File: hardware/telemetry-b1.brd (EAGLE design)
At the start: 63.5 x 76.2 mm, 119 parts, among them IC1 COPERNICUSSMD, IC10 TPS70933, IC2 TPS70933, IC4 STM32L073CZT6, IC5 TPS62160, IC6 HX1, IC7 LMP7702, IC9 HIH9131, J1 I2C1, J10 TEMP_BAT, J11 DNP, J12 INSOL, J13 SMA_EDGE, J2 I2C2, J3 SMA_EDGE, J4 USD-SOCKET, J5 BAT, J6 SMA_EDGE, J7 SMA_EDGE, J8 TEMP_GPS, J9 TEMP_HOT, K1 ARE104H, K2 ARE104H, Q1 AO3400A, Q2 AO3400A, U1 LTC3105, U2 INA219, Y1 32768, Y2 8M

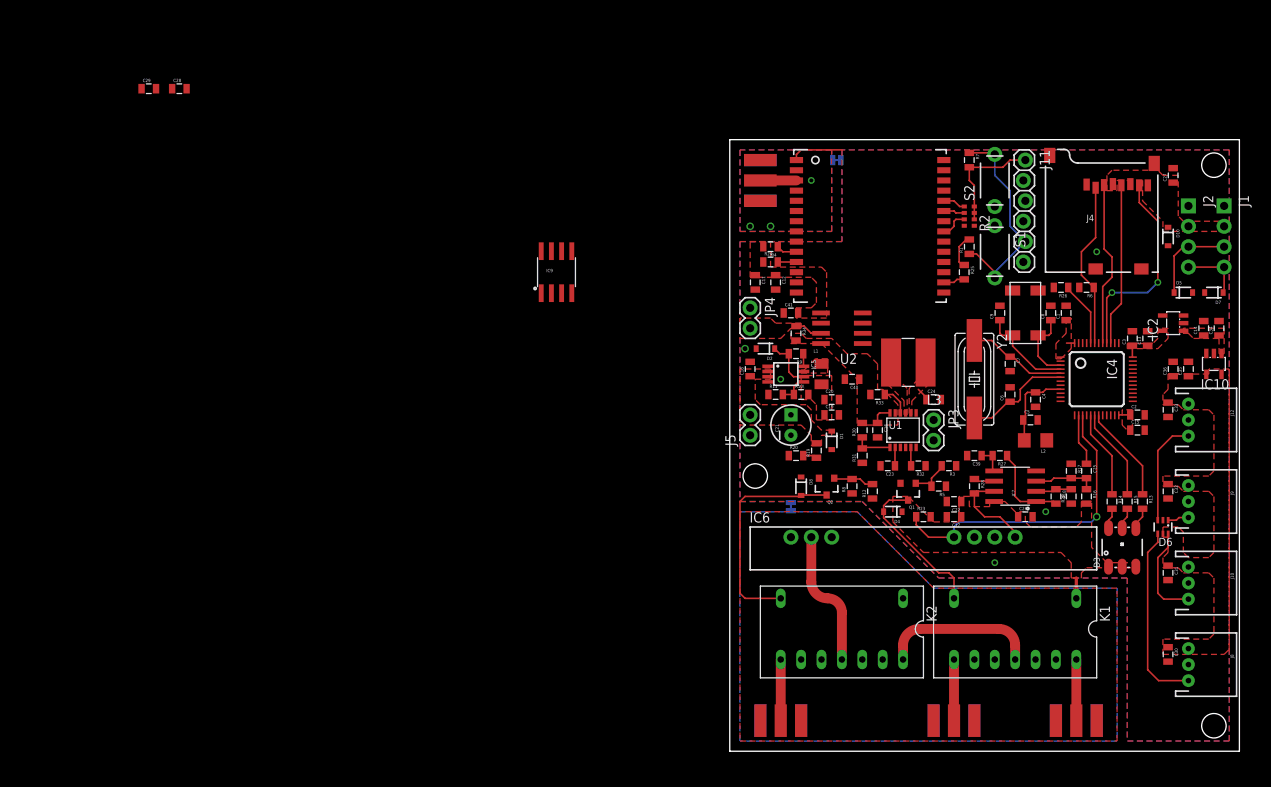
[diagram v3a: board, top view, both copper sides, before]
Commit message: Work on layout on beta PCB. Need to swap i2c and swd headers
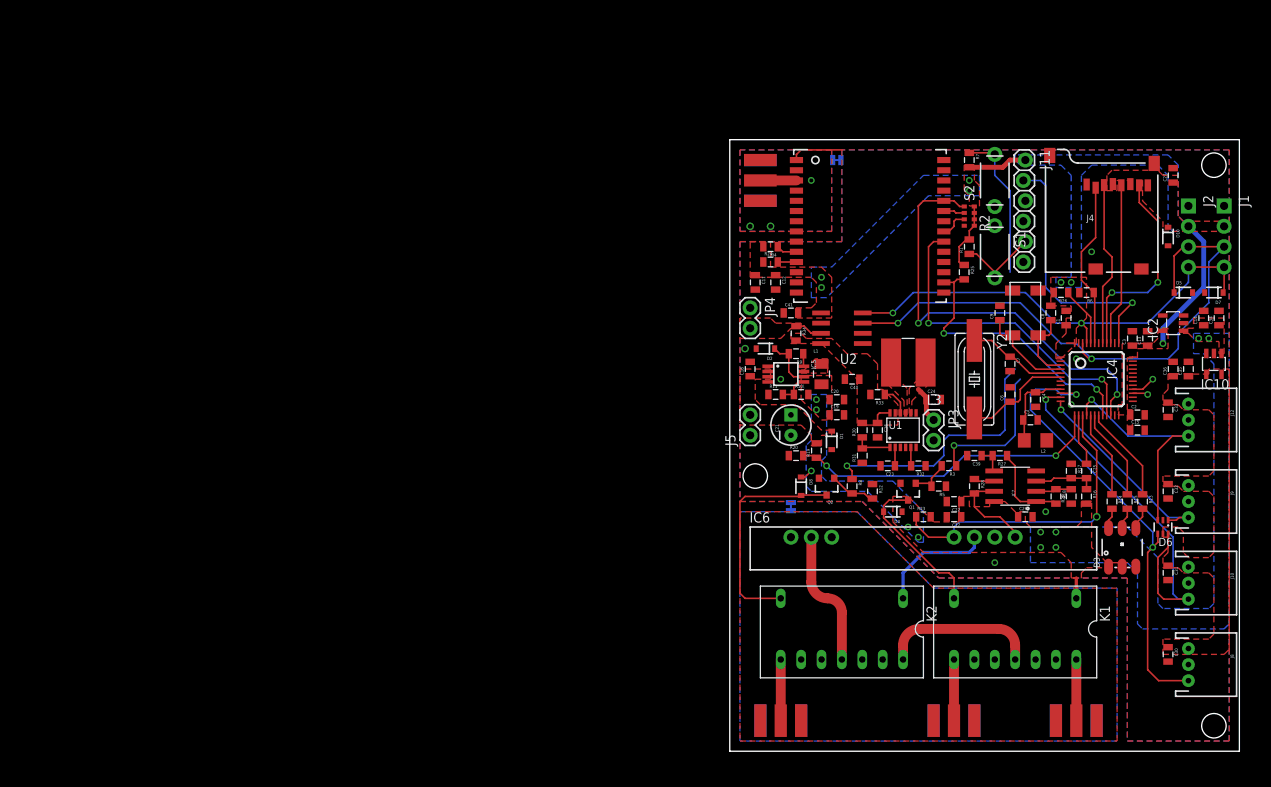
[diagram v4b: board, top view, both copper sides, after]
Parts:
- removed C28, C29: 0.1u, SparkFun-Passives:0805
- removed IC9: HIH9131, SparkFun-AnalogIC:SOIC8
- added U$2: (no value), HAB:GARAGE
- added U$5: (no value), HAB:MSFT_LOGO
- moved FRAME2 85.9 mm to (0.00, 77.5)
- moved FRAME1 84.6 mm to (1.27, 77.5)
- moved C14 1.27 mm to (59.1, 54.0)
- moved C34 1.27 mm to (61.0, 54.0)
- moved C19 0.64 mm to (13.3, 41.9)
- moved C20 0.64 mm to (13.3, 43.8)
- moved C1 0.63 mm to (41.9, 54.0)
- moved R26 0.63 mm to (41.3, 57.1)
- moved R6 0.63 mm to (44.5, 57.1)
- turned R12 to 270 degrees
- turned R8 to 270 degrees
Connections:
- removed net AL_L: IC9.6
- removed net VCORE: C28.1, IC9.1
- net 3.3V: now also R2.1
- net CSHUM: no longer IC9.3
- net GND: no longer C28.2, C29.2, IC9.2
- net MISO: no longer IC9.5
- net SCK: no longer IC9.4
- net VS: no longer C29.1, IC9.8
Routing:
- net SDA: track 11.3 -> 72.7 mm, vias 0 -> 2
- net GPSRX: track 2.84 -> 54.4 mm, vias 0 -> 2
- net SCL: track 7.67 -> 57.6 mm, vias 0 -> 2
- net GPSTX: track 0.00 -> 40.9 mm, vias 0 -> 2
- net VDIV: track 1.75 -> 39.6 mm, vias 0 -> 2
- net RS1: track 0.00 -> 35.7 mm, vias 0 -> 2
- net TEMPB: track 12.0 -> 47.0 mm, vias 0 -> 1
- net TEMPG: track 23.1 -> 56.7 mm, vias 0 -> 2
- net SWCLK: track 0.00 -> 33.1 mm, vias 0 -> 1
- net XSTBY: track 2.69 -> 35.1 mm, vias 0 -> 2
- net PHOTO: track 2.66 -> 25.2 mm, vias 0 -> 1
- net RS0: track 0.00 -> 20.0 mm, vias 0 -> 2
- net 5V: track 8.91 -> 25.1 mm, vias 0 -> 11
- net INSOL: track 13.2 -> 29.4 mm, vias 0 -> 1
- net 3.3V: track 22.0 -> 34.6 mm, vias 0 -> 7
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- added copper zone on layer 16, net 3.3V
- added copper zone on layer 16, net 5V

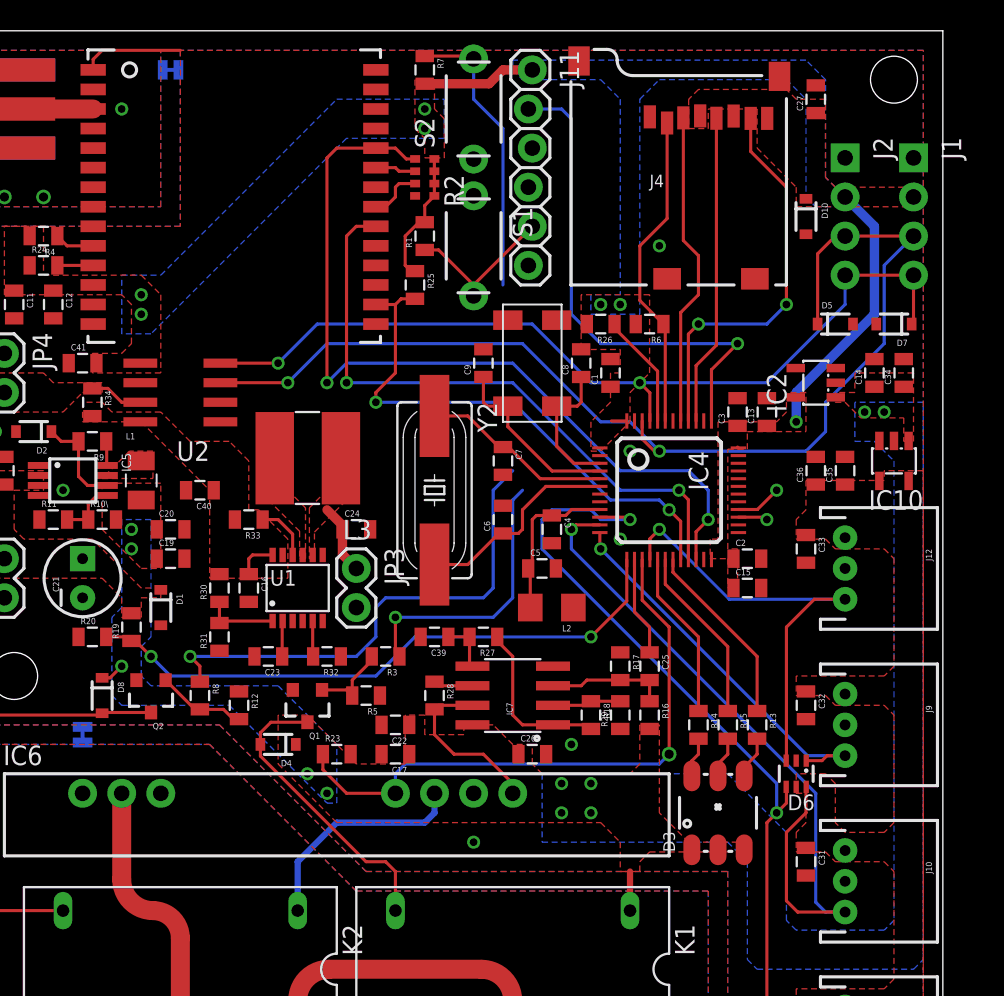
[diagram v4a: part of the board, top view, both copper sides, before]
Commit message: Finish routing all traces on beta board. Needs a silkscreen pass.
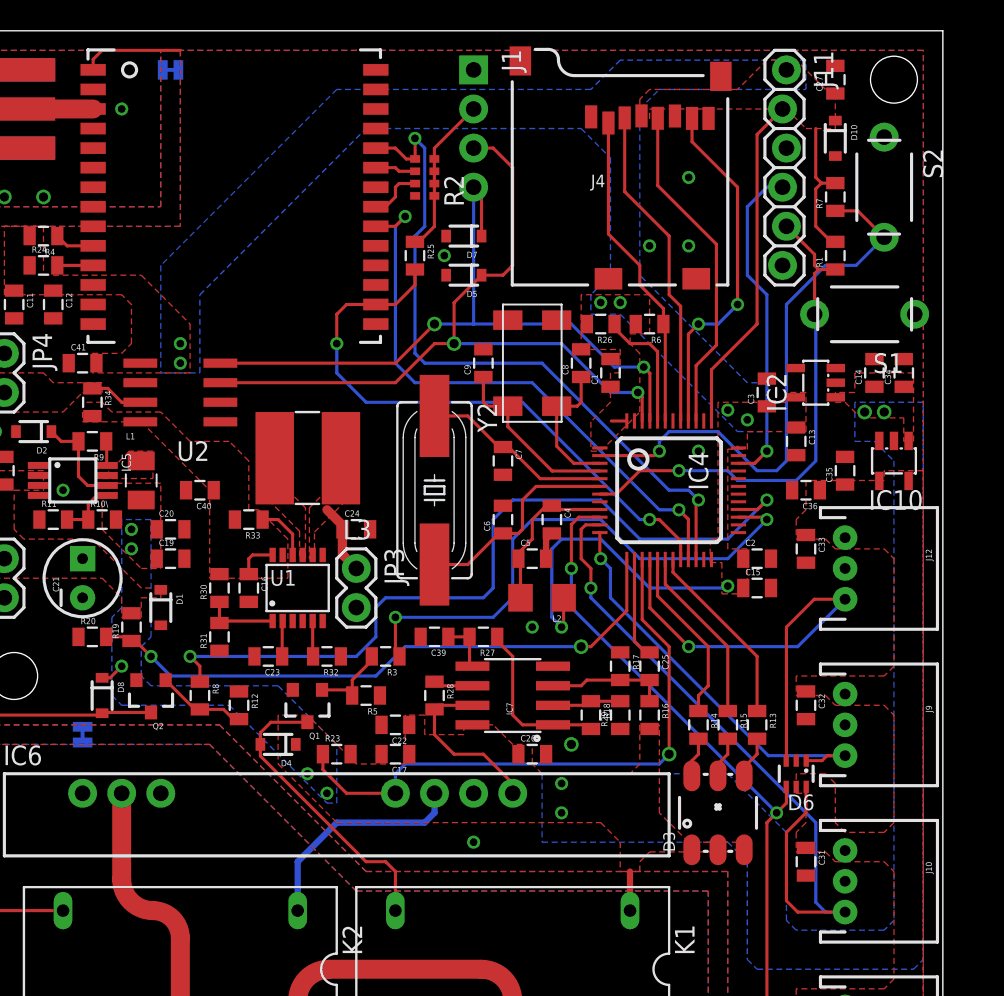
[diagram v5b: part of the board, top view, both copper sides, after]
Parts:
- removed J2: I2C2, SparkFun-Connectors:1X04_NO_SILK
- moved U$5 71.9 mm to (20.3, 16.5)
- moved J1 29.1 mm to (33.0, 73.7)
- moved D7 28.5 mm to (32.4, 62.9)
- moved R7 27.9 mm to (56.5, 65.4), turned to 90 degrees
- moved S2 27.1 mm to (59.7, 66.0), turned to 270 degrees
- moved R1 26.7 mm to (56.5, 61.6)
- moved S1 25.8 mm to (58.4, 57.8), turned to 180 degrees
- moved D5 24.3 mm to (32.4, 60.3), turned to 180 degrees
- moved U$2 16.8 mm to (21.0, 68.6)
- moved J11 16.5 mm to (53.3, 73.7)
- moved D10 5.43 mm to (56.5, 69.2)
- moved J4 3.81 mm to (35.6, 59.7)
- moved C13 2.69 mm to (54.0, 49.5), turned to 270 degrees
- moved C3 2.29 mm to (52.1, 52.7)
- moved R25 1.91 mm to (29.2, 61.6)
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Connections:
- net 3.3V: no longer J2.2
- net GND: no longer J2.1
- net SCL: no longer J2.4
- net SDA: no longer J2.3
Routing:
- net SDA: track 72.7 -> 48.3 mm
- net !RST!: track 10.9 -> 32.8 mm, vias 0 -> 1
- net SWDIO: track 0.00 -> 21.4 mm, vias 0 -> 1
- net BTN: track 18.7 -> 36.7 mm, vias 0 -> 1
- net RS1: track 35.7 -> 51.5 mm
- net RS0: track 20.0 -> 35.7 mm
- net SCL: track 57.6 -> 45.7 mm
- net SWCLK: track 33.1 -> 22.2 mm, vias 1 -> 0
- net GPSRX: track 54.4 -> 45.0 mm
- net TEMPG: track 56.7 -> 49.4 mm
- net 3.3V: track 34.6 -> 41.1 mm, vias 7 -> 8
- net XSTBY: track 35.1 -> 38.8 mm
- net GPSTX: track 40.9 -> 37.8 mm
- net MISO: track 25.9 -> 22.9 mm
- net INSOL: track 29.4 -> 31.4 mm
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
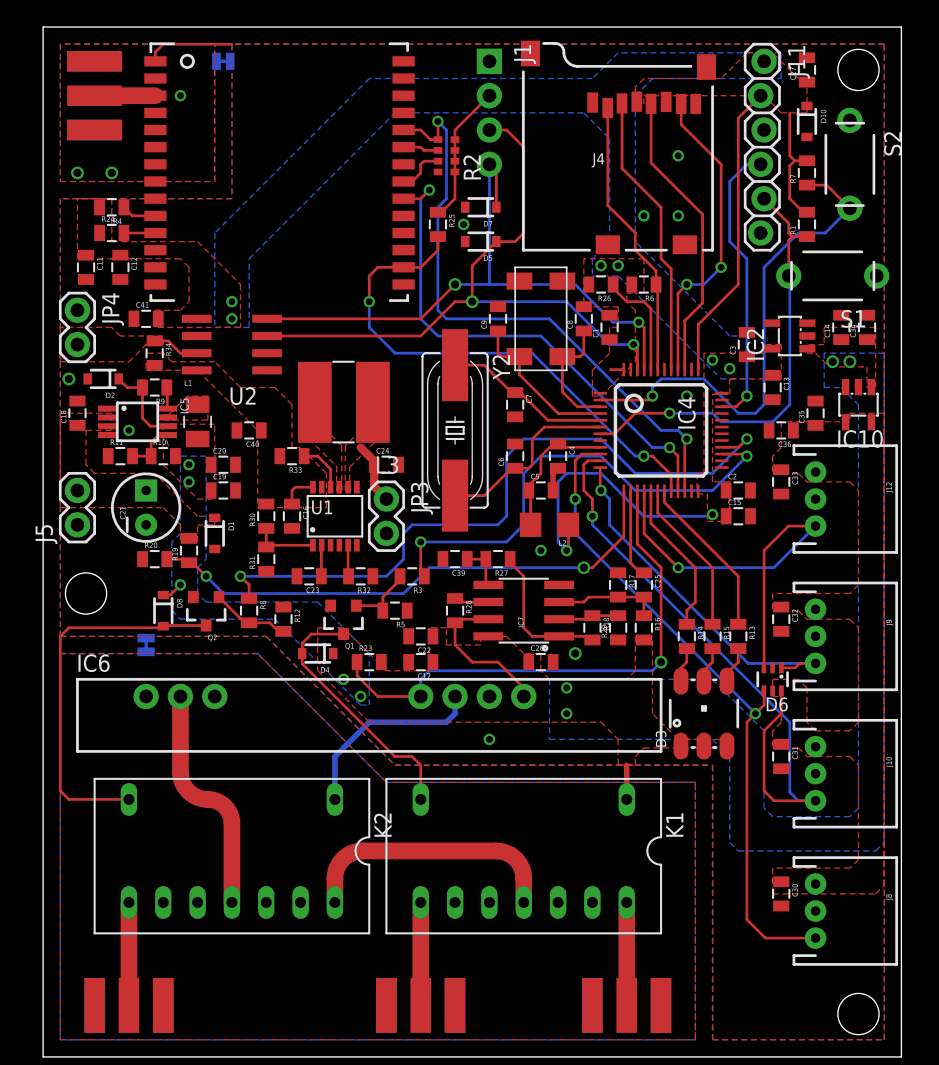
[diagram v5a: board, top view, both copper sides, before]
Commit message: Silkscreen gloss on beta board
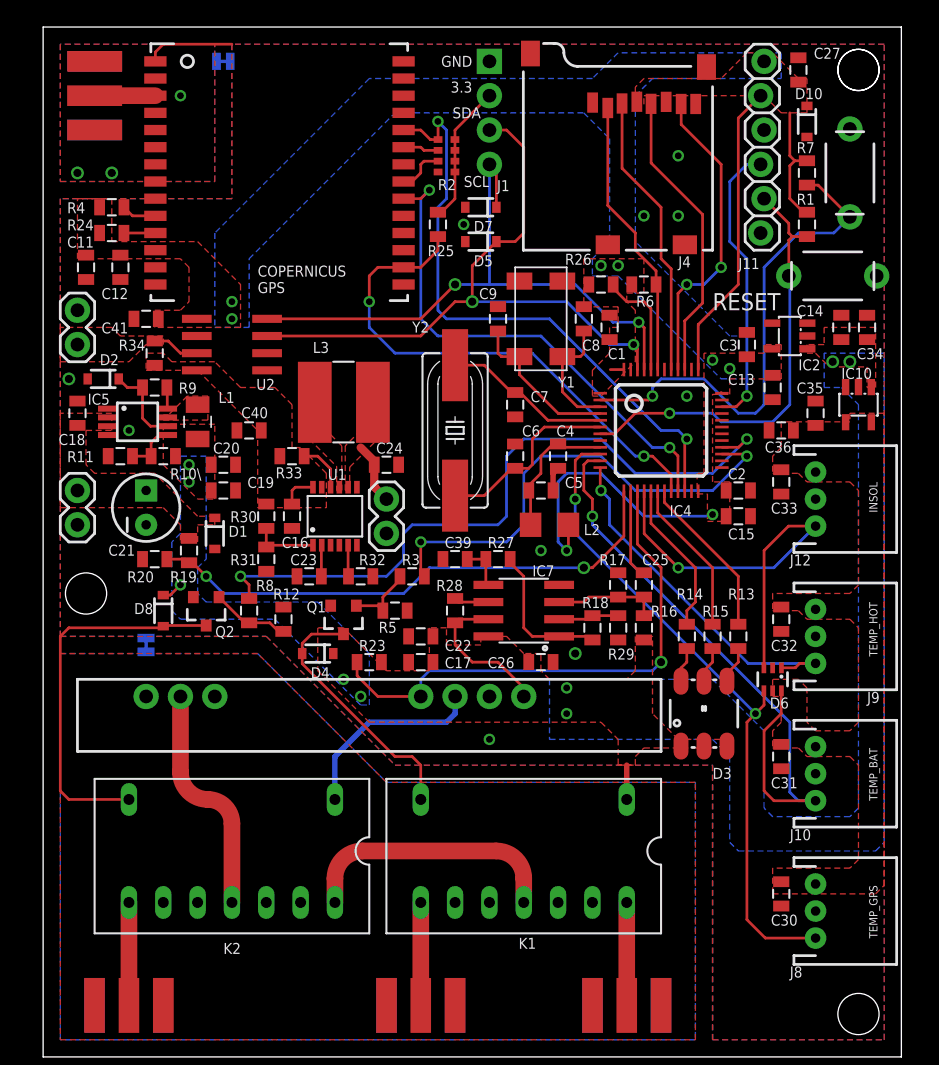
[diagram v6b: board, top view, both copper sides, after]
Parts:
- J1: value I2C1 -> I2C
- moved S2 0.64 mm to (59.7, 65.4)
- moved C27 0.63 mm to (55.9, 73.0)
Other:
- board text added: "3.3"
- board text added: "COPERNICUS GPS"
- board text added: "Contact ~STCARLSO 301 956 5041"
- board text added: "GND"
- board text added: "HAB Project"
- board text added: "Microsoft Maker Garage"
- board text added: "RESET"
- board text added: "SCL"
- board text added: "SDA"
- board text added: "Telemetry Rev 3B"
- board text added: "Y1"
